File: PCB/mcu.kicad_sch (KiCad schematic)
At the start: 36 parts

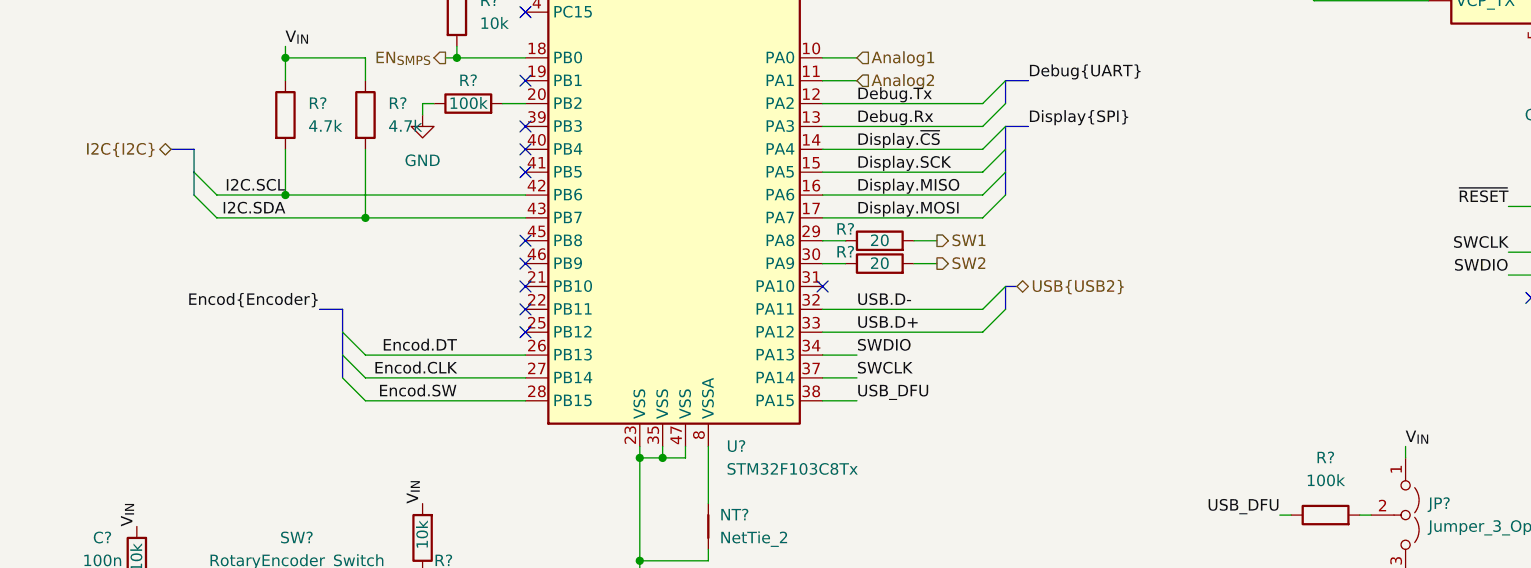
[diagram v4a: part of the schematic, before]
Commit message: update pin config stm32
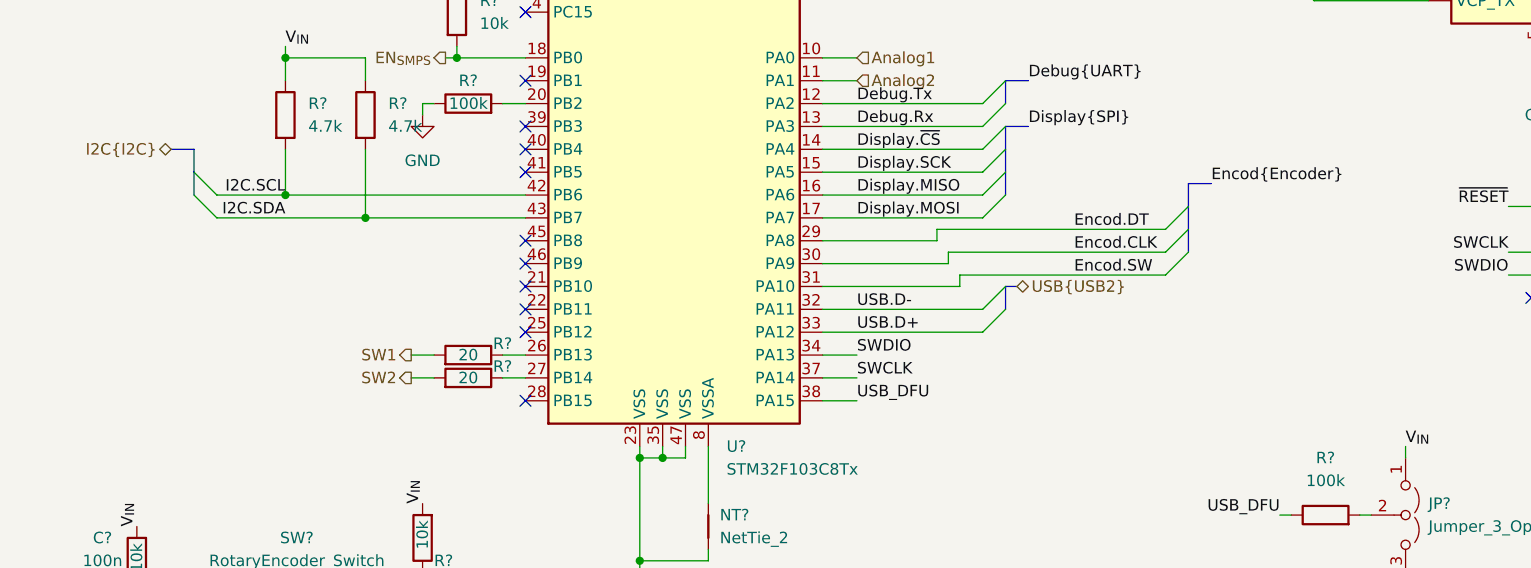
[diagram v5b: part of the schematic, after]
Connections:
- net Encod.CLK: now also U?.30 (PA9); no longer U?.27 (PB14)
- net Encod.DT: now also U?.29 (PA8); no longer U?.26 (PB13)
- net Encod.SW: now also U?.31 (PA10); no longer U?.28 (PB15)
- net at R?.1: now also U?.26 (PB13); no longer U?.29 (PA8)
- net at R?.1: now also U?.27 (PB14); no longer U?.30 (PA9)
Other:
- moved on the sheet: R?
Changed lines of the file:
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@@
   (no_connect (at 130.81 90.17))
   (no_connect (at 130.81 87.63))
+  (no_connect (at 130.81 133.35))
   (no_connect (at 130.81 85.09))
   (no_connect (at 130.81 118.11))
@@
   (no_connect (at 130.81 107.95))
   (no_connect (at 130.81 125.73))
-  (no_connect (at 163.83 120.65))
   (no_connect (at 130.81 115.57))
   (no_connect (at 231.14 73.66))
@@
   (no_connect (at 130.81 105.41))
   (no_connect (at 242.57 121.92))
-  (bus_entry (at 110.49 130.81) (size 2.54 2.54)
+  (bus_entry (at 204.47 116.84) (size -2.54 2.54)
     (stroke (width 0) (type default) (color 0 0 0 0))
   )
@@
     (stroke (width 0) (type default) (color 0 0 0 0))
   )
-  (bus_entry (at 110.49 125.73) (size 2.54 2.54)
+  (bus_entry (at 204.47 111.76) (size -2.54 2.54)
     (stroke (width 0) (type default) (color 0 0 0 0))
   )
@@
     (stroke (width 0) (type default) (color 0 0 0 0))
   )
-  (bus_entry (at 110.49 128.27) (size 2.54 2.54)
+  (bus_entry (at 204.47 114.3) (size -2.54 2.54)
     (stroke (width 0) (type default) (color 0 0 0 0))
   )
@@
     (stroke (width 0) (type default) (color 0 0 0 0))
   )
+  (wire (pts (xy 163.83 115.57) (xy 176.53 115.57))
+    (stroke (width 0) (type default) (color 0 0 0 0))
+  )
   (bus (pts (xy 215.9 83.82) (xy 215.9 86.36))
     (stroke (width 0) (type default) (color 0 0 0 0))
@@
     (stroke (width 0) (type default) (color 0 0 0 0))
   )
+  (wire (pts (xy 179.07 120.65) (xy 163.83 120.65))
+    (stroke (width 0) (type default) (color 0 0 0 0))
+  )
   (wire (pts (xy 34.29 35.56) (xy 34.29 36.83))
     (stroke (width 0) (type default) (color 0 0 0 0))
@@
     (stroke (width 0) (type default) (color 0 0 0 0))
   )
-  (wire (pts (xy 113.03 128.27) (xy 130.81 128.27))
-    (stroke (width 0) (type default) (color 0 0 0 0))
-  )
   (wire (pts (xy 163.83 105.41) (xy 181.61 105.41))
     (stroke (width 0) (type default) (color 0 0 0 0))
@@
     (stroke (width 0) (type default) (color 0 0 0 0))
   )
-  (wire (pts (xy 173.99 115.57) (xy 176.53 115.57))
+  (wire (pts (xy 120.65 128.27) (xy 118.11 128.27))
     (stroke (width 0) (type default) (color 0 0 0 0))
   )
@@
     (stroke (width 0) (type default) (color 0 0 0 0))
   )
+  (wire (pts (xy 177.8 118.11) (xy 177.8 116.84))
+    (stroke (width 0) (type default) (color 0 0 0 0))
+  )
   (wire (pts (xy 243.84 95.25) (xy 243.84 96.52))
     (stroke (width 0) (type default) (color 0 0 0 0))
@@
     (stroke (width 0) (type default) (color 0 0 0 0))
   )
+  (wire (pts (xy 176.53 114.3) (xy 176.53 115.57))
+    (stroke (width 0) (type default) (color 0 0 0 0))
+  )
   (wire (pts (xy 78.74 158.75) (xy 97.79 158.75))
     (stroke (width 0) (type default) (color 0 0 0 0))
@@
     (stroke (width 0) (type default) (color 0 0 0 0))
   )
-  (wire (pts (xy 163.83 115.57) (xy 166.37 115.57))
+  (wire (pts (xy 130.81 128.27) (xy 128.27 128.27))
     (stroke (width 0) (type default) (color 0 0 0 0))
   )
@@
     (stroke (width 0) (type default) (color 0 0 0 0))
   )
-  (wire (pts (xy 173.99 118.11) (xy 176.53 118.11))
+  (wire (pts (xy 120.65 130.81) (xy 118.11 130.81))
     (stroke (width 0) (type default) (color 0 0 0 0))
   )
@@
     (stroke (width 0) (type default) (color 0 0 0 0))
   )
+  (wire (pts (xy 179.07 119.38) (xy 179.07 120.65))
+    (stroke (width 0) (type default) (color 0 0 0 0))
+  )
   (wire (pts (xy 57.15 35.56) (xy 68.58 35.56))
     (stroke (width 0) (type default) (color 0 0 0 0))
@@
     (stroke (width 0) (type default) (color 0 0 0 0))
   )
+  (wire (pts (xy 179.07 119.38) (xy 201.93 119.38))
+    (stroke (width 0) (type default) (color 0 0 0 0))
+  )
   (wire (pts (xy 115.57 176.53) (xy 115.57 156.21))
     (stroke (width 0) (type default) (color 0 0 0 0))
@@
     (stroke (width 0) (type default) (color 0 0 0 0))
   )
-  (bus (pts (xy 110.49 123.19) (xy 110.49 125.73))
+  (bus (pts (xy 204.47 109.22) (xy 204.47 111.76))
     (stroke (width 0) (type default) (color 0 0 0 0))
   )
@@
     (stroke (width 0) (type default) (color 0 0 0 0))
   )
+  (wire (pts (xy 177.8 116.84) (xy 201.93 116.84))
+    (stroke (width 0) (type default) (color 0 0 0 0))
+  )
   (wire (pts (xy 57.15 45.72) (xy 68.58 45.72))
     (stroke (width 0) (type default) (color 0 0 0 0))
@@
     (stroke (width 0) (type default) (color 0 0 0 0))
   )
-  (wire (pts (xy 113.03 133.35) (xy 130.81 133.35))
-    (stroke (width 0) (type default) (color 0 0 0 0))
-  )
   (bus (pts (xy 105.41 172.72) (xy 105.41 176.53))
     (stroke (width 0) (type default) (color 0 0 0 0))
@@
     (stroke (width 0) (type default) (color 0 0 0 0))
   )
-  (bus (pts (xy 110.49 128.27) (xy 110.49 130.81))
+  (bus (pts (xy 204.47 114.3) (xy 204.47 116.84))
     (stroke (width 0) (type default) (color 0 0 0 0))
   )
@@
     (stroke (width 0) (type default) (color 0 0 0 0))
   )
-  (wire (pts (xy 113.03 130.81) (xy 130.81 130.81))
-    (stroke (width 0) (type default) (color 0 0 0 0))
-  )
   (wire (pts (xy 104.14 110.49) (xy 130.81 110.49))
     (stroke (width 0) (type default) (color 0 0 0 0))
@@
     (stroke (width 0) (type default) (color 0 0 0 0))
   )
+  (wire (pts (xy 176.53 114.3) (xy 201.93 114.3))
+    (stroke (width 0) (type default) (color 0 0 0 0))
+  )
   (wire (pts (xy 80.01 35.56) (xy 68.58 35.56))
     (stroke (width 0) (type default) (color 0 0 0 0))
@@
     (stroke (width 0) (type default) (color 0 0 0 0))
   )
-  (bus (pts (xy 110.49 125.73) (xy 110.49 128.27))
+  (bus (pts (xy 204.47 111.76) (xy 204.47 114.3))
     (stroke (width 0) (type default) (color 0 0 0 0))
   )
@@
     (stroke (width 0) (type default) (color 0 0 0 0))
   )
-  (bus (pts (xy 107.95 123.19) (xy 110.49 123.19))
+  (bus (pts (xy 207.01 109.22) (xy 204.47 109.22))
     (stroke (width 0) (type default) (color 0 0 0 0))
   )
@@
     (stroke (width 0) (type default) (color 0 0 0 0))
   )
-  (wire (pts (xy 163.83 118.11) (xy 166.37 118.11))
+  (wire (pts (xy 130.81 130.81) (xy 128.27 130.81))
+    (stroke (width 0) (type default) (color 0 0 0 0))
+  )
+  (wire (pts (xy 163.83 118.11) (xy 177.8 118.11))
     (stroke (width 0) (type default) (color 0 0 0 0))
   )
@@
     (effects (font (size 1.27 1.27)) (justify left bottom))
   )
-  (label "Encod.CLK" (at 123.19 130.81 180)
-    (effects (font (size 1.27 1.27)) (justify right bottom))
-  )
-  (label "Encod{Encoder}" (at 107.95 123.19 180)
-    (effects (font (size 1.27 1.27)) (justify right bottom))
+  (label "Encod.CLK" (at 191.77 116.84 0)
+    (effects (font (size 1.27 1.27)) (justify left bottom))
+  )
+  (label "Encod{Encoder}" (at 207.01 109.22 0)
+    (effects (font (size 1.27 1.27)) (justify left bottom))
   )
   (label "~{RESET}" (at 240.03 111.76 180)
@@
     (effects (font (size 1.27 1.27)) (justify right bottom))
   )
-  (label "Encod.DT" (at 123.19 128.27 180)
-    (effects (font (size 1.27 1.27)) (justify right bottom))
+  (label "Encod.DT" (at 191.77 114.3 0)
+    (effects (font (size 1.27 1.27)) (justify left bottom))
   )
   (label "I2C.SDA" (at 104.14 113.03 180)
@@
     (effects (font (size 1.27 1.27)) (justify right bottom))
   )
-  (label "Encod.SW" (at 123.19 133.35 180)
-    (effects (font (size 1.27 1.27)) (justify right bottom))
+  (label "Encod.SW" (at 191.77 119.38 0)
+    (effects (font (size 1.27 1.27)) (justify left bottom))
   )
   (label "V_{IN}" (at 243.84 55.88 0)
@@
     (effects (font (size 1.27 1.27)) (justify right))
   )
-  (hierarchical_label "SW1" (shape output) (at 176.53 115.57 0)
-    (effects (font (size 1.27 1.27)) (justify left))
-  )
-  (hierarchical_label "SW2" (shape output) (at 176.53 118.11 0)
-    (effects (font (size 1.27 1.27)) (justify left))
+  (hierarchical_label "SW1" (shape output) (at 118.11 128.27 180)
+    (effects (font (size 1.27 1.27)) (justify right))
+  )
+  (hierarchical_label "SW2" (shape output) (at 118.11 130.81 180)
+    (effects (font (size 1.27 1.27)) (justify right))
   )
   (hierarchical_label "Analog1" (shape input) (at 167.64 95.25 0)
@@
     (pin "1")
   )
-  (symbol (lib_id "Device:R") (at 170.18 118.11 90) (unit 1)
+  (symbol (lib_id "Device:R") (at 124.46 130.81 270) (mirror x) (unit 1)
     (in_bom yes) (on_board yes)
-    (property "Reference" "R?" (id 0) (at 166.37 116.84 90))
-    (property "Value" "20" (id 1) (at 170.18 118.11 90))
-    (property "Footprint" "" (id 2) (at 170.18 119.888 90)
-      (effects (font (size 1.27 1.27)) hide)
-    )
-    (property "Datasheet" "~" (id 3) (at 170.18 118.11 0)
+    (property "Reference" "R?" (id 0) (at 128.27 129.54 90))
+    (property "Value" "20" (id 1) (at 124.46 130.81 90))
+    (property "Footprint" "" (id 2) (at 124.46 132.588 90)
+      (effects (font (size 1.27 1.27)) hide)
+    )
+    (property "Datasheet" "~" (id 3) (at 124.46 130.81 0)
       (effects (font (size 1.27 1.27)) hide)
     )
@@
     (pin "2")
   )
-  (symbol (lib_id "Device:R") (at 170.18 115.57 90) (unit 1)
+  (symbol (lib_id "Device:R") (at 124.46 128.27 270) (mirror x) (unit 1)
     (in_bom yes) (on_board yes)
-    (property "Reference" "R?" (id 0) (at 166.37 114.3 90))
-    (property "Value" "20" (id 1) (at 170.18 115.57 90))
-    (property "Footprint" "" (id 2) (at 170.18 117.348 90)
-      (effects (font (size 1.27 1.27)) hide)
-    )
-    (property "Datasheet" "~" (id 3) (at 170.18 115.57 0)
-      (effects (font (size 1.27 1.27)) hide)
-    )
+    (property "Reference" "R?" (id 0) (at 128.27 127 90))
+    (property "Value" "20" (id 1) (at 124.46 128.27 90))
+    (property "Footprint" "" (id 2) (at 124.46 130.048 90)
+      (effects (font (size 1.27 1.27)) hide)
+    )
+    (property "Datasheet" "~" (id 3) (at 124.46 128.27 0)
+      (effects (font (size 1.27 1.27)) hide)
+    )

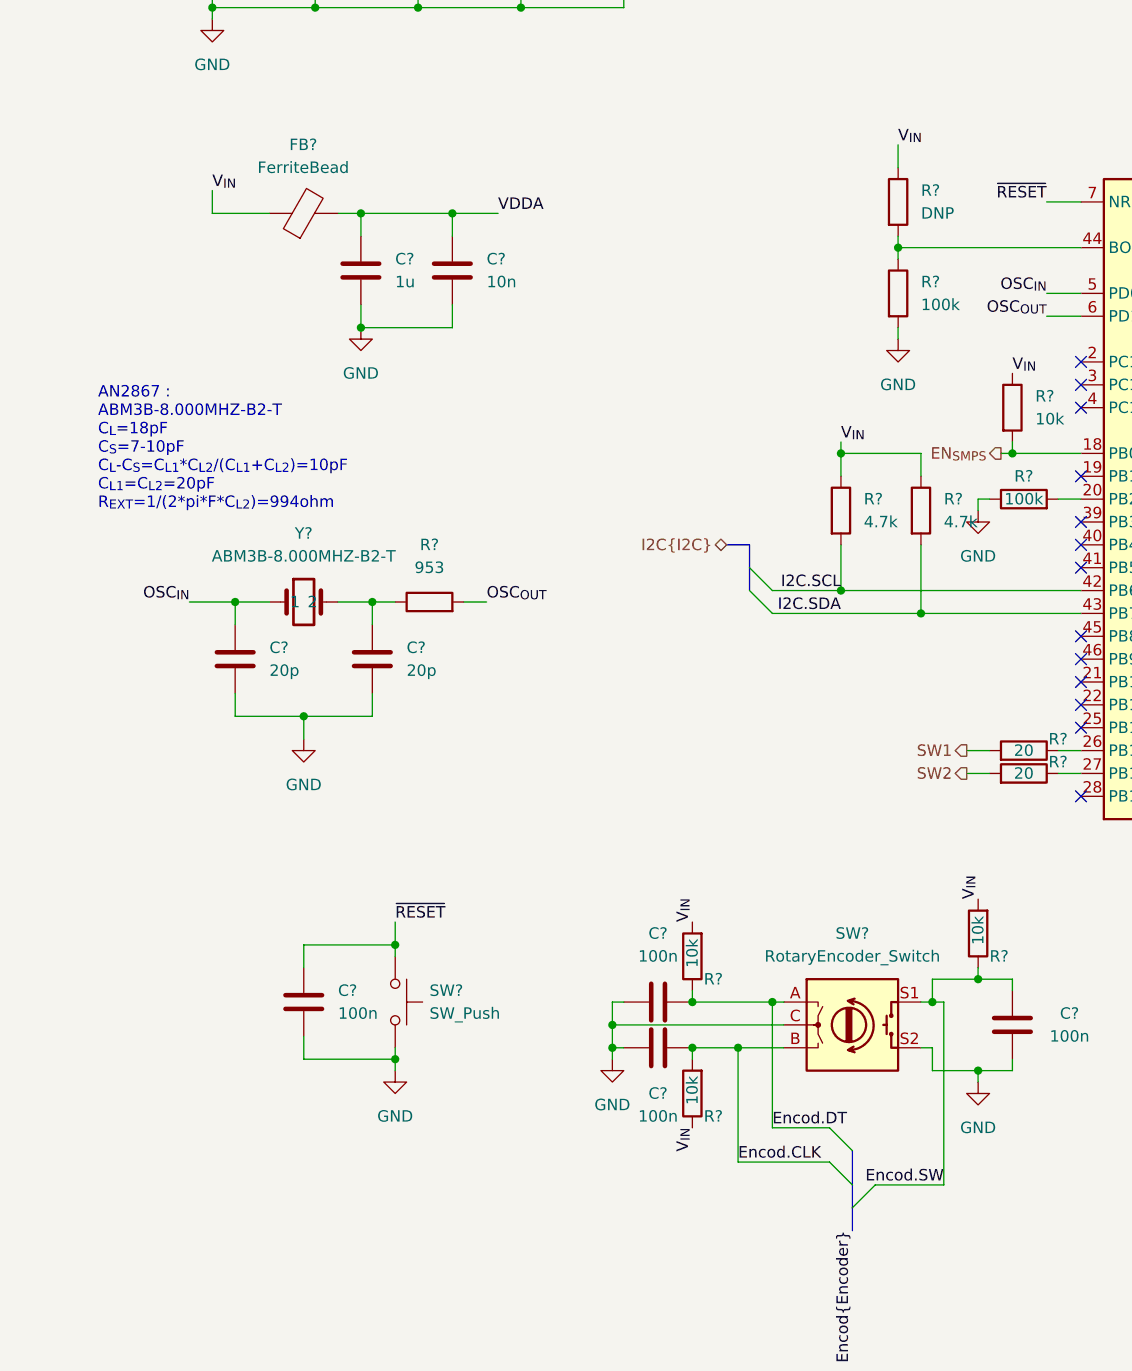
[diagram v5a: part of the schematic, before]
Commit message: upgrade usb protection + kicad 7
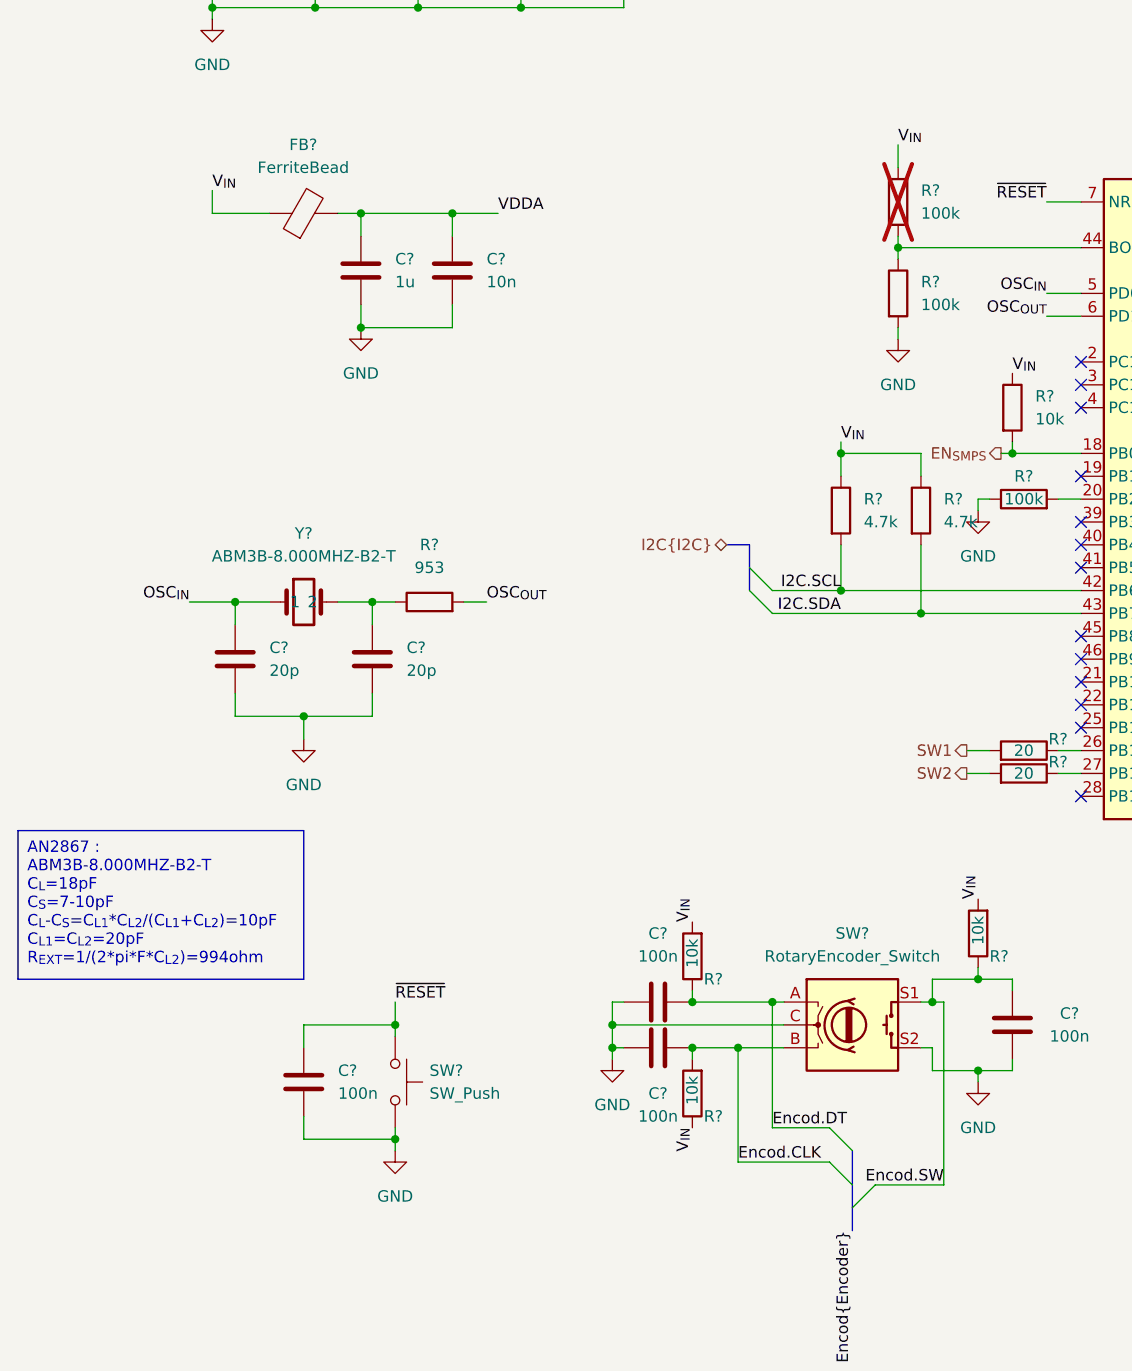
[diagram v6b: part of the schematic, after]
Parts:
- R?: value DNP -> 100k; now not fitted
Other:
- note removed: "AN2867 : ABM3B-8.000MHZ-B2-T C_{L}=18pF C_{S}=7-10pF C_{L}-C_{S}=C_{L1}*C_{L2}/(C_{L1}+C_{L2})=10pF C_{L1}=C_{L2}=20pF R_{EXT}=1/(2*pi*F*C_{L2})=994ohm"
- moved on the sheet: C?, SW?
